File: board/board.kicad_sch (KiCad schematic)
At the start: 38 parts, among them J1 Conn_01x25_Socket, J2 Conn_01x25_Socket, J5 PJ-320B, J6 Screw_Terminal_01x02, J7 Screw_Terminal_01x02, J8 Screw_Terminal_01x02

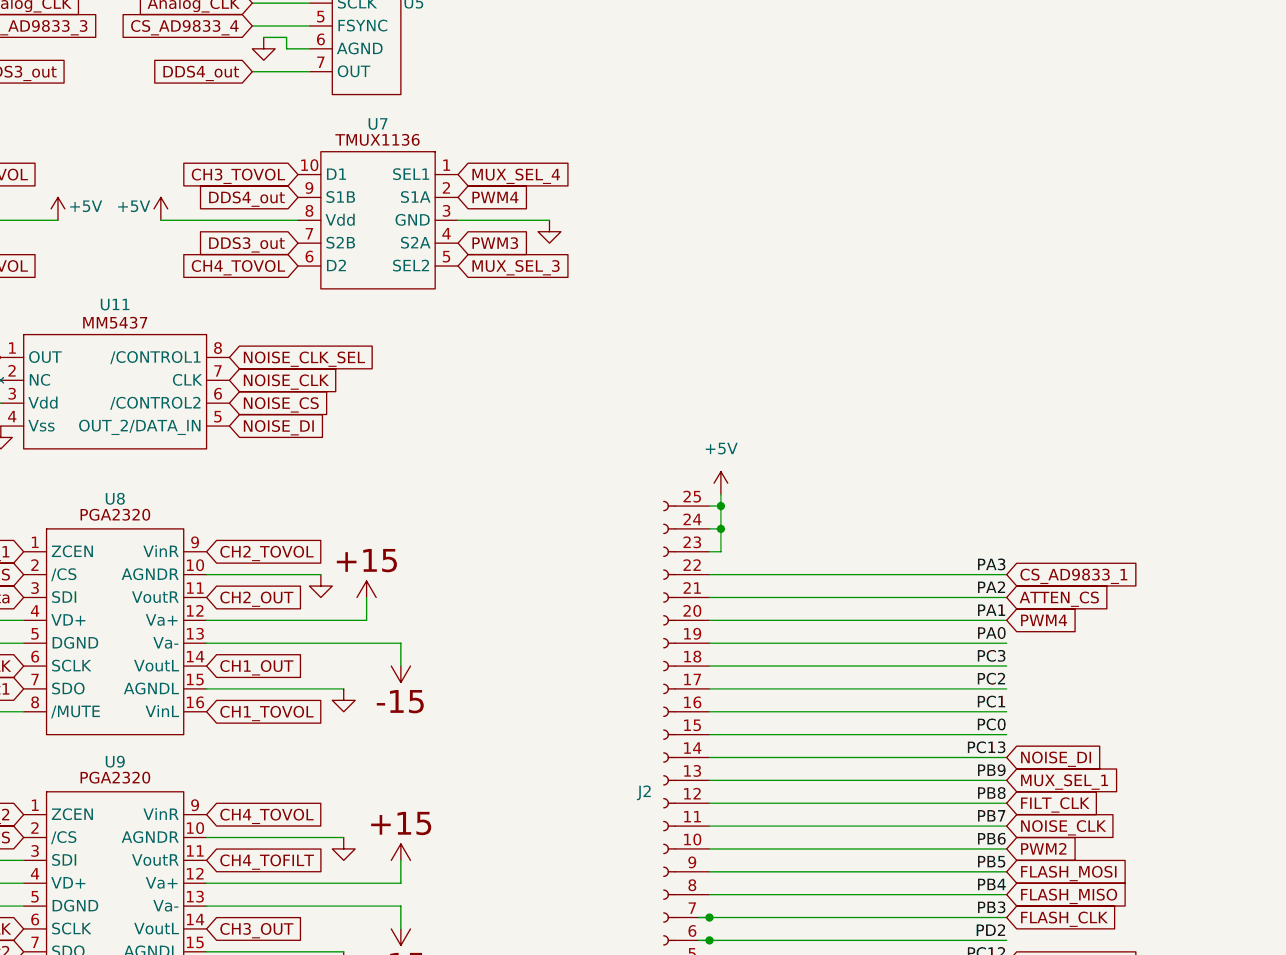
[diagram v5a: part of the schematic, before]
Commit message: reassign noise pins so that noise clock and noise data in are on the same GPIO port
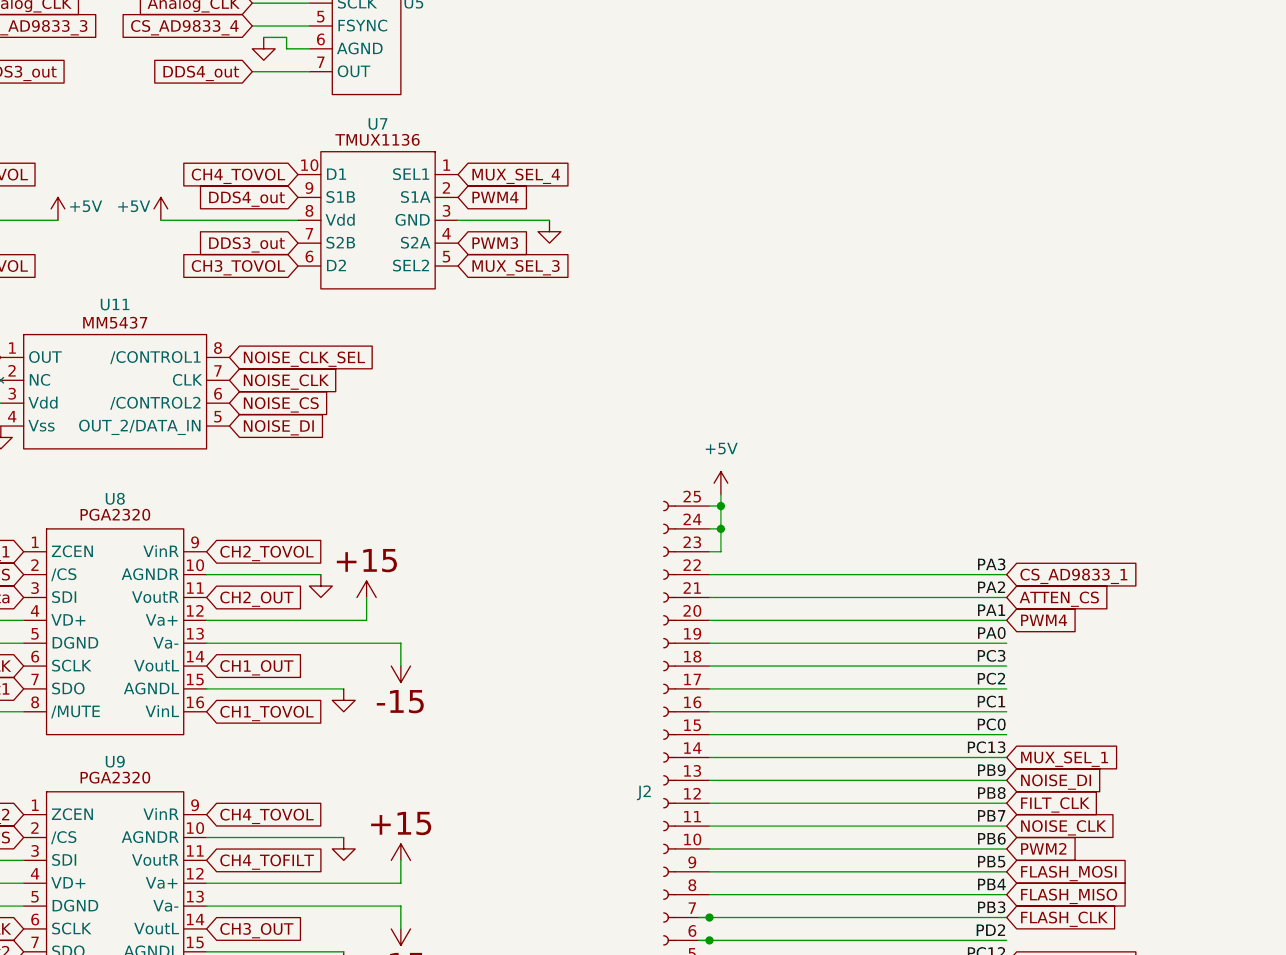
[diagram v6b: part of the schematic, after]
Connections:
- net CH3_TOVOL: now also U7.6 (D2); no longer U7.10 (D1)
- net CH4_TOVOL: now also U7.10 (D1); no longer U7.6 (D2)
- net MUX_SEL_1: now also J2.14 (Pin_14); no longer J2.13 (Pin_13)
- net NOISE_DI: now also J2.13 (Pin_13); no longer J2.14 (Pin_14)

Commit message: add caps on power lines, start tracing
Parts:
- added C1, C10, C11, C12, C13, C14, C15, C16, C17, C18, C19, C2, C20, C21, C22, C23, C3, C4, C5, C6, C7, C8, C9: 0.22uF_0603_25V, 4ms_Capacitor:C_0603, symbol 4ms_Capacitor:0.22uF_0603_25V
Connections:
- net PD2 is gone; now on net FLASH_CS: J2.6 (Pin_6)
- net +3.3V: now also C13.1
- net +5V: now also C1.1, C14.1, C15.1, C18.1, C2.1, C22.1, C23.1, C3.1, C4.1, C5.1, C6.1, C7.1, C8.1
- net FLASH_CS: no longer J1.14 (Pin_14)
- net GND: now also C1.2, C10.2, C11.2, C12.2, C13.2, C14.2, C15.2, C16.2, C17.2, C18.2, C19.2, C2.2, C20.2, C21.2, C22.2, C23.2, C3.2, C4.2, C5.2, C6.2, C7.2, C8.2, C9.2
- net P,+15: now also C11.1, C16.1, C19.1, C9.1
- net P,-15: now also C10.1, C12.1, C17.1, C20.1
- net P,-5: now also C21.1
- new net PB14/adc4_in4: J1.14 (Pin_14)

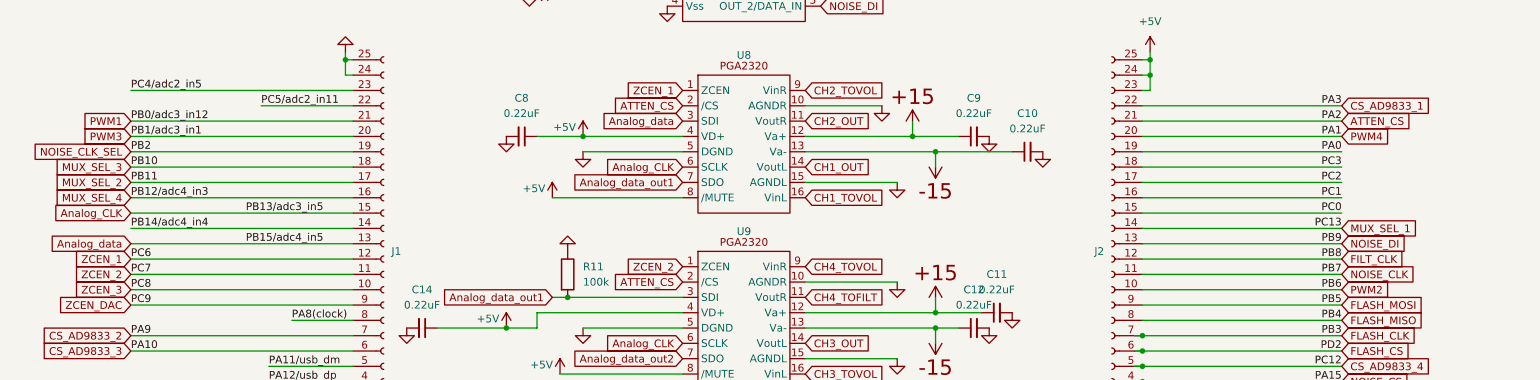
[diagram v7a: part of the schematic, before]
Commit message: traced (changed some CS and mux select pins to make tracing easier)
Dude that's horrible PCB...
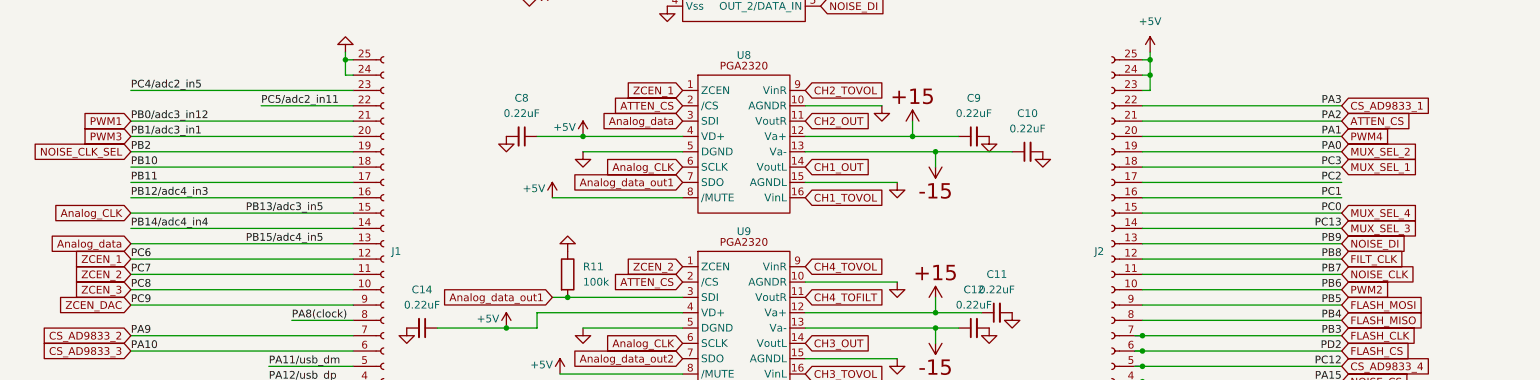
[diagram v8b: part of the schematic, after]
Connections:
- net PA0 is gone; now on net MUX_SEL_2: J2.19 (Pin_19)
- net PC0 is gone; now on net MUX_SEL_4: J2.15 (Pin_15)
- net PC3 is gone; now on net MUX_SEL_1: J2.18 (Pin_18)
- net MUX_SEL_1: no longer J2.14 (Pin_14)
- net MUX_SEL_2: no longer J1.17 (Pin_17)
- net MUX_SEL_3: now also J2.14 (Pin_14); no longer J1.18 (Pin_18)
- net MUX_SEL_4: no longer J1.16 (Pin_16)
- new net PB10: J1.18 (Pin_18)
- new net PB11: J1.17 (Pin_17)
- new net PB12/adc4_in3: J1.16 (Pin_16)
